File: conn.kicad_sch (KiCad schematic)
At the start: 14 parts, among them J10 PwrOut, J11 IO2, J12 I^{2}C, J13 USB_C_Receptacle, J14 IO1, J15 IO0, J4 GND, J5 Field24V, J6 Amphenol RJHSE5380, J7 Amphenol RJHSE5380, J8 CAN, J9 CAN

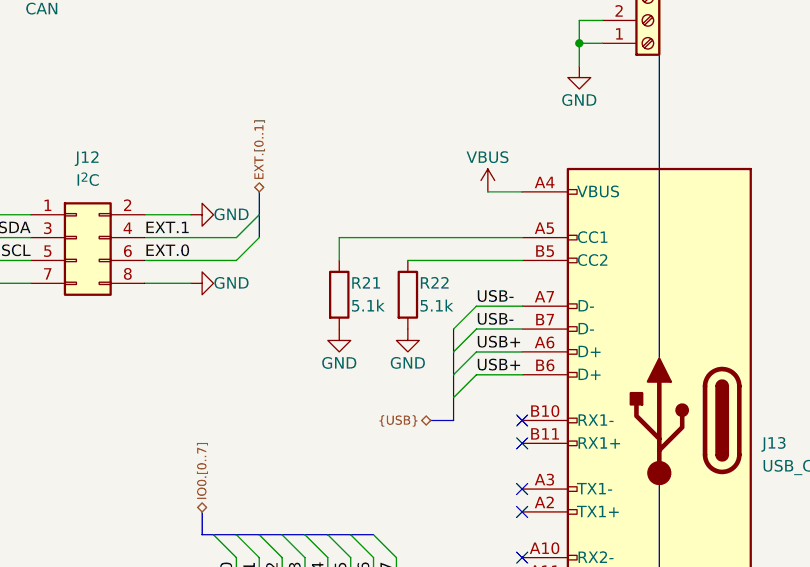
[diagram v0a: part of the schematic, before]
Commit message: rev1.1: Add I2C pullups
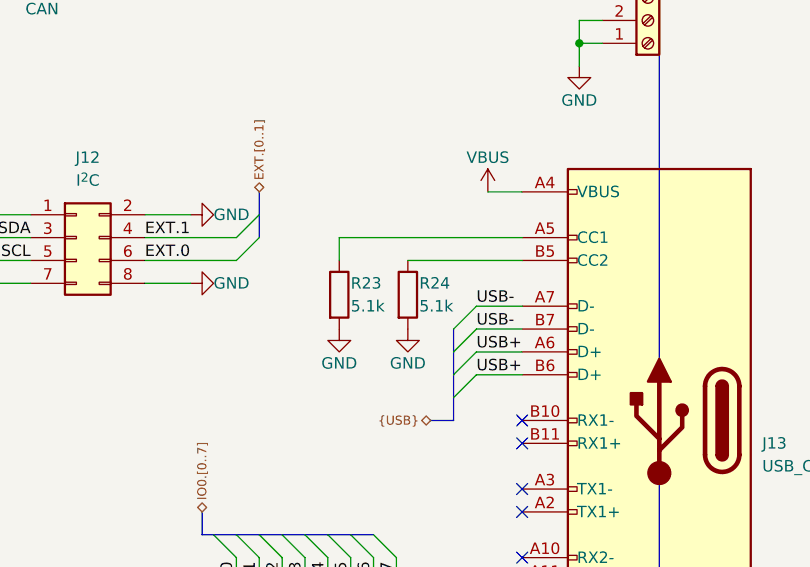
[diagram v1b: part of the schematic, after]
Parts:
- renumbered R21 to R23, R22 to R24
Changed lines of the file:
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@@
   (title_block
     (title "[canbrd] CAN/RS485 IO board")
-    (date "2022-02-24")
-    (rev "1.0")
+    (date "2022-03-18")
+    (rev "1.1")
   )
   (junction (at 121.92 44.45) (diameter 0) (color 0 0 0 0)
@@
   (symbol (lib_id "power:GND") (at 101.6 35.56 0) (unit 1)
     (in_bom yes) (on_board yes)
-    (property "Reference" "#PWR0133" (id 0) (at 101.6 41.91 0)
+    (property "Reference" "#PWR0135" (id 0) (at 101.6 41.91 0)
       (effects (font (size 1.27 1.27)) hide)
     )
@@
   (symbol (lib_id "power:+3.3V") (at 196.85 64.77 0) (unit 1)
     (in_bom yes) (on_board yes)
-    (property "Reference" "#PWR0139" (id 0) (at 196.85 68.58 0)
+    (property "Reference" "#PWR0141" (id 0) (at 196.85 68.58 0)
       (effects (font (size 1.27 1.27)) hide)
     )
@@
   (symbol (lib_id "power:+5V") (at 201.93 64.77 0) (unit 1)
     (in_bom yes) (on_board yes)
-    (property "Reference" "#PWR0140" (id 0) (at 201.93 68.58 0)
+    (property "Reference" "#PWR0142" (id 0) (at 201.93 68.58 0)
       (effects (font (size 1.27 1.27)) hide)
     )
@@
   (symbol (lib_id "power:GND") (at 163.83 104.14 90) (unit 1)
     (in_bom yes) (on_board yes)
-    (property "Reference" "#PWR0145" (id 0) (at 170.18 104.14 0)
+    (property "Reference" "#PWR0147" (id 0) (at 170.18 104.14 0)
       (effects (font (size 1.27 1.27)) hide)
     )
@@
   (symbol (lib_id "power:GND") (at 140.97 111.76 270) (unit 1)
     (in_bom yes) (on_board yes)
-    (property "Reference" "#PWR0146" (id 0) (at 134.62 111.76 0)
+    (property "Reference" "#PWR0148" (id 0) (at 134.62 111.76 0)
       (effects (font (size 1.27 1.27)) hide)
     )
@@
   (symbol (lib_id "power:GND") (at 121.92 45.72 0) (unit 1)
     (in_bom yes) (on_board yes)
-    (property "Reference" "#PWR0136" (id 0) (at 121.92 52.07 0)
+    (property "Reference" "#PWR0138" (id 0) (at 121.92 52.07 0)
       (effects (font (size 1.27 1.27)) hide)
     )
@@
   (symbol (lib_id "power:GND") (at 187.96 116.84 0) (unit 1)
     (in_bom yes) (on_board yes)
-    (property "Reference" "#PWR0149" (id 0) (at 187.96 123.19 0)
+    (property "Reference" "#PWR0151" (id 0) (at 187.96 123.19 0)
       (effects (font (size 1.27 1.27)) hide)
     )
@@
   (symbol (lib_id "power:GND") (at 140.97 104.14 270) (unit 1)
     (in_bom yes) (on_board yes)
-    (property "Reference" "#PWR0144" (id 0) (at 134.62 104.14 0)
+    (property "Reference" "#PWR0146" (id 0) (at 134.62 104.14 0)
       (effects (font (size 1.27 1.27)) hide)
     )
@@
   (symbol (lib_id "Device:R") (at 187.96 113.03 0) (unit 1)
     (in_bom yes) (on_board yes)
-    (property "Reference" "R22" (id 0) (at 189.23 111.76 0)
+    (property "Reference" "R24" (id 0) (at 189.23 111.76 0)
       (effects (font (size 1.27 1.27)) (justify left))
     )
@@
   (symbol (lib_id "power:GND") (at 153.67 45.72 0) (unit 1)
     (in_bom yes) (on_board yes)
-    (property "Reference" "#PWR0138" (id 0) (at 153.67 52.07 0)
+    (property "Reference" "#PWR0140" (id 0) (at 153.67 52.07 0)
       (effects (font (size 1.27 1.27)) hide)
     )
@@
   (symbol (lib_id "power:GND") (at 207.01 87.63 0) (unit 1)
     (in_bom yes) (on_board yes)
-    (property "Reference" "#PWR0142" (id 0) (at 207.01 93.98 0)
+    (property "Reference" "#PWR0144" (id 0) (at 207.01 93.98 0)
       (effects (font (size 1.27 1.27)) hide)
     )
@@
   (symbol (lib_id "power:GND") (at 163.83 111.76 90) (unit 1)
     (in_bom yes) (on_board yes)
-    (property "Reference" "#PWR0147" (id 0) (at 170.18 111.76 0)
+    (property "Reference" "#PWR0149" (id 0) (at 170.18 111.76 0)
       (effects (font (size 1.27 1.27)) hide)
     )
@@
   (symbol (lib_id "power:+24V") (at 207.01 64.77 0) (unit 1)
     (in_bom yes) (on_board yes)
-    (property "Reference" "#PWR0141" (id 0) (at 207.01 68.58 0)
+    (property "Reference" "#PWR0143" (id 0) (at 207.01 68.58 0)
       (effects (font (size 1.27 1.27)) hide)
     )
@@
   (symbol (lib_id "power:GND") (at 111.76 45.72 0) (unit 1)
     (in_bom yes) (on_board yes)
-    (property "Reference" "#PWR0135" (id 0) (at 111.76 52.07 0)
+    (property "Reference" "#PWR0137" (id 0) (at 111.76 52.07 0)
       (effects (font (size 1.27 1.27)) hide)
     )
@@
   (symbol (lib_id "Device:R") (at 180.34 113.03 0) (unit 1)
     (in_bom yes) (on_board yes)
-    (property "Reference" "R21" (id 0) (at 181.61 111.76 0)
+    (property "Reference" "R23" (id 0) (at 181.61 111.76 0)
       (effects (font (size 1.27 1.27)) (justify left))
     )
@@
   (symbol (lib_id "power:GND") (at 215.9 167.64 0) (unit 1)
     (in_bom yes) (on_board yes)
-    (property "Reference" "#PWR0150" (id 0) (at 215.9 173.99 0)
+    (property "Reference" "#PWR0152" (id 0) (at 215.9 173.99 0)
       (effects (font (size 1.27 1.27)) hide)
     )
@@
   (symbol (lib_id "power:GND") (at 180.34 116.84 0) (unit 1)
     (in_bom yes) (on_board yes)
-    (property "Reference" "#PWR0148" (id 0) (at 180.34 123.19 0)
+    (property "Reference" "#PWR0150" (id 0) (at 180.34 123.19 0)
       (effects (font (size 1.27 1.27)) hide)
     )
@@
   (symbol (lib_id "power:GND") (at 133.35 35.56 0) (unit 1)
     (in_bom yes) (on_board yes)
-    (property "Reference" "#PWR0134" (id 0) (at 133.35 41.91 0)
+    (property "Reference" "#PWR0136" (id 0) (at 133.35 41.91 0)
       (effects (font (size 1.27 1.27)) hide)
     )
@@
   (symbol (lib_id "power:VBUS") (at 196.85 101.6 0) (unit 1)
     (in_bom yes) (on_board yes)
-    (property "Reference" "#PWR0143" (id 0) (at 196.85 105.41 0)
+    (property "Reference" "#PWR0145" (id 0) (at 196.85 105.41 0)
       (effects (font (size 1.27 1.27)) hide)
     )
@@
   (symbol (lib_id "power:GND") (at 223.52 167.64 0) (unit 1)
     (in_bom yes) (on_board yes)
-    (property "Reference" "#PWR0151" (id 0) (at 223.52 173.99 0)
+    (property "Reference" "#PWR0153" (id 0) (at 223.52 173.99 0)
       (effects (font (size 1.27 1.27)) hide)
     )
@@
   (symbol (lib_id "power:GND") (at 143.51 45.72 0) (unit 1)
     (in_bom yes) (on_board yes)
-    (property "Reference" "#PWR0137" (id 0) (at 143.51 52.07 0)
+    (property "Reference" "#PWR0139" (id 0) (at 143.51 52.07 0)
       (effects (font (size 1.27 1.27)) hide)
     )
@@
   (symbol (lib_id "power:GND") (at 182.88 33.02 0) (unit 1)
     (in_bom yes) (on_board yes)
-    (property "Reference" "#PWR0132" (id 0) (at 182.88 39.37 0)
-      (effects (font (size 1.27 1.27)) hide)
-    )
+    (property "Reference" "#PWR0134" (id 0) (at 182.88 39.37 0)
+      (effects (font (size 1.27 1.27)) hide)
+    )

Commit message: lots changed
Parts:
- removed J12: I^{2}C, Connector_PinHeader_2.54mm:PinHeader_2x04_P2.54mm_Vertical_SMD, symbol Connector_Generic:Conn_02x04_Odd_Even
- removed J6, J7: Amphenol RJHSE5380, Connector_RJ:RJ45_Amphenol_RJHSE5380, symbol Connector:RJ45_Shielded
- added J5: (no value), symbol Connector:RJ45_LED_Shielded_x2
- J11: renamed from J14; value IO1 -> DIO
- J12: renamed from J15; value IO0 -> AIO
- J9: renamed from J11; value IO2 -> OUT
- renumbered J13 to J10, J4 to J3, J5 to J4, J8 to J6, J9 to J7, J10 to J8, R23 to R41, R24 to R42
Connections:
- net IO0.1 is gone; now on net GND: J12.2 (Pin_2)
- net IO0.4 is gone; now on net GND: J12.5 (Pin_5)
- net IO0.7 is gone; now on net GND: J12.8 (Pin_8)
- net CANH: now also J6.2 (Pin_2), J7.2 (Pin_2), J5.1, J5.13; no longer J6.1 (Pin_1), J7.1 (Pin_1)
- net CANL: now also J6.1 (Pin_1), J7.1 (Pin_1), J5.14, J5.2; no longer J6.2 (Pin_2), J7.2 (Pin_2)
- net Field24V: now also J5.20, J5.8
- net GND: now also J5.15, J5.18, J5.19, J5.3, J5.6, J5.7, J5.SH, J5.SH
- net IO0.0 renamed VIO
- net IO0.2 renamed IO8
- net IO0.3 renamed IO9
- net IO0.5 renamed IO10
- net IO0.6 renamed IO11
- net IO1.0 renamed IO0
- net IO1.1 renamed IO1
- net IO1.2 renamed IO2
- net IO1.3 renamed IO3
- net IO1.4 renamed IO4
- net IO1.5 renamed IO5
- net IO1.6 renamed IO6
- net IO1.7 renamed IO7
- net IO2.0 renamed OUT0
- net IO2.1 renamed OUT1
- net IO2.2 renamed OUT2
- net IO2.3 renamed OUT3
- net IO2.4 renamed OUT4
- net IO2.5 renamed OUT5
- net IO2.6 renamed OUT6
- net IO2.7 renamed OUT7
- no-connect marks 14 -> 22
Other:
- moved on the sheet: J6, J7

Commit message: things changed
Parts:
- added J7: CANGND, canbrd_conn:NH0210x0xxxxG, symbol Connector:Screw_Terminal_01x02
- J5: value (none) -> RJ45_LED_Shielded_x2; footprint (none) -> canbrd_conn:RJ45_Amphenol_RJHSE5380-02
- renumbered J9 to J10, J10 to J11, J11 to J12, J12 to J13, J7 to J8, J8 to J9, R41 to R55, R42 to R56
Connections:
- net Field24V: now also J5.16, J5.4
- net GND: now also J5.17, J5.5; no longer J5.15, J5.18, J5.3, J5.6, J5.SH, J5.SH
- new net GNDISO: J5.15, J5.3, J7.1 (Pin_1), J7.2 (Pin_2)

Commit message: isolate and other stuff
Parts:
- removed J6, J8: CAN, canbrd_conn:NH0210x0xxxxG, symbol Connector:Screw_Terminal_01x02
- removed J7: CANGND, canbrd_conn:NH0210x0xxxxG, symbol Connector:Screw_Terminal_01x02
- added J10: VIO2, canbrd_conn:NH0210x0xxxxG, symbol Connector:Screw_Terminal_01x02
- added J7, J8: CAN, canbrd_conn:NH0310x0xxxxG, symbol Connector:Screw_Terminal_01x03
- renumbered J9 to J6, J10 to J9, R55 to R60, R56 to R61
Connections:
- net CANH: now also J7.3 (Pin_3), J8.3 (Pin_3)
- net CANL: now also J7.1 (Pin_1), J8.1 (Pin_1)
- net GND: now also J10.2 (Pin_2)
- net GNDISO: now also J7.2 (Pin_2), J8.2 (Pin_2)
- new net VIO2: J10.1 (Pin_1)
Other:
- title: [canbrd] CAN/RS485 IO board -> [canbrd] CAN IO board

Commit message: things changed
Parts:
- added J13: GND, canbrd_conn:NH0210x0xxxxG, symbol Connector:Screw_Terminal_01x02
- added J15: IO_IDC, 71922:71922-126, symbol Connector_Generic:Conn_02x13_Odd_Even
- J11: symbol Connector:USB_C_Receptacle -> canbrd_conn:USB_C_Receptacle_noVbus
- J14: renamed from J13; value AIO -> AIN
- J5: symbol Connector:RJ45_LED_Shielded_x2 -> canbrd_conn:8P8C_noLED_Shielded_x2
- renumbered R60 to R69, R61 to R70
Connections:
- net +5V: now also J15.20 (Pin_20), J15.22 (Pin_22)
- net GND: now also J13.2 (Pin_2), J15.13 (Pin_13), J15.14 (Pin_14), J15.16 (Pin_16), J15.18 (Pin_18); no longer J14.2 (Pin_2), J14.5 (Pin_5), J14.8 (Pin_8)
- net GNDISO: now also J5.SH, J5.SH
- net IO0: now also J15.2 (Pin_2)
- net IO1: now also J15.4 (Pin_4)
- net IO2: now also J15.1 (Pin_1)
- net IO3: now also J15.3 (Pin_3)
- net IO4: now also J15.5 (Pin_5)
- net IO5: now also J15.7 (Pin_7)
- net IO6: now also J15.9 (Pin_9)
- net IO7: now also J15.11 (Pin_11)
- net VIO: now also J13.1 (Pin_1), J15.10 (Pin_10), J15.12 (Pin_12); no longer J14.1 (Pin_1)
- net +3V3 renamed +3.3V
- net +3.3V: now also J15.6 (Pin_6), J15.8 (Pin_8)
- net IO10 renamed AIN2
- net AIN2: now also J15.25 (Pin_25)
- net IO11 renamed AIN1
- net AIN1: now also J15.24 (Pin_24)
- net IO8 renamed AIN5
- net AIN5: now also J15.19 (Pin_19)
- net IO9 renamed AIN4
- net AIN4: now also J15.21 (Pin_21)
- removed net VBUS: J11.A4 (VBUS), J11.A9 (VBUS), J11.B4 (VBUS), J11.B9 (VBUS)
- new net AIN0: J14.8 (Pin_8), J15.26 (Pin_26)
- new net AIN3: J14.5 (Pin_5), J15.23 (Pin_23)
- new net AIN6: J14.2 (Pin_2), J15.17 (Pin_17)
- new net AIN7: J14.1 (Pin_1), J15.15 (Pin_15)
- no-connect marks 22 -> 12
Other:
- moved on the sheet: J10, J12, J14, J3, J4, J6, J7, J8, J9, R69, R70
